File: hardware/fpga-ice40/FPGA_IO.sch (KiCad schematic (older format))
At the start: 1 part, among them U1 iCE40HX4K-TQ144

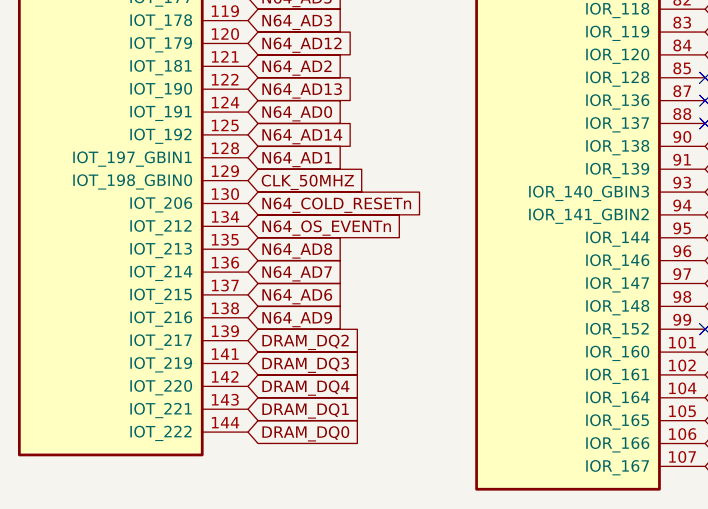
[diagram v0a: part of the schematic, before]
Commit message: Finish layout of power mux
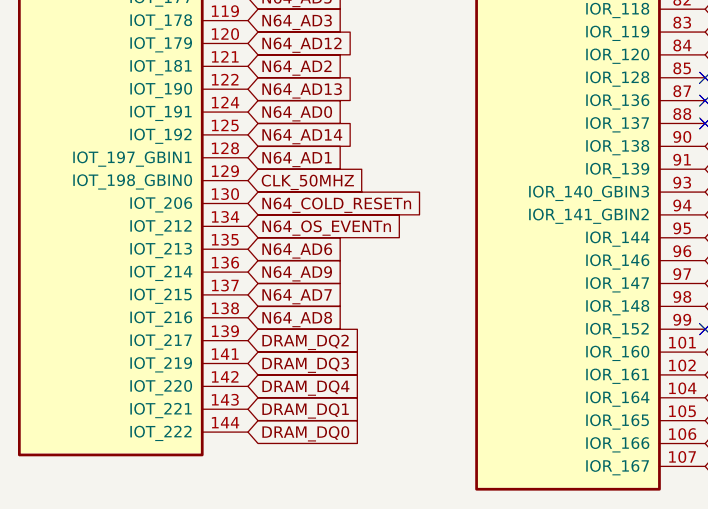
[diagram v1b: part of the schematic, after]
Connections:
- net N64_AD6: now also U1.135 (IOT_213); no longer U1.137 (IOT_215)
- net N64_AD7: now also U1.137 (IOT_215); no longer U1.136 (IOT_214)
- net N64_AD8: now also U1.138 (IOT_216); no longer U1.135 (IOT_213)
- net N64_AD9: now also U1.136 (IOT_214); no longer U1.138 (IOT_216)
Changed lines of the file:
@@
 Text GLabel 8850 3850 2    50   Input ~ 0
 DRAM_DQ8
-Text GLabel 2850 4750 2    50   Input ~ 0
+Text GLabel 2850 4850 2    50   Input ~ 0
 N64_AD7
-Text GLabel 2850 4850 2    50   Input ~ 0
+Text GLabel 2850 4650 2    50   Input ~ 0
 N64_AD6
 Text GLabel 2850 3550 2    50   Input ~ 0
@@
 Text GLabel 2850 4450 2    50   Input ~ 0
 N64_COLD_RESETn
-Text GLabel 2850 4650 2    50   Input ~ 0
+Text GLabel 2850 4950 2    50   Input ~ 0
 N64_AD8
-Text GLabel 2850 4950 2    50   Input ~ 0
+Text GLabel 2850 4750 2    50   Input ~ 0
 N64_AD9
 Text GLabel 2850 3450 2    50   Input ~ 0

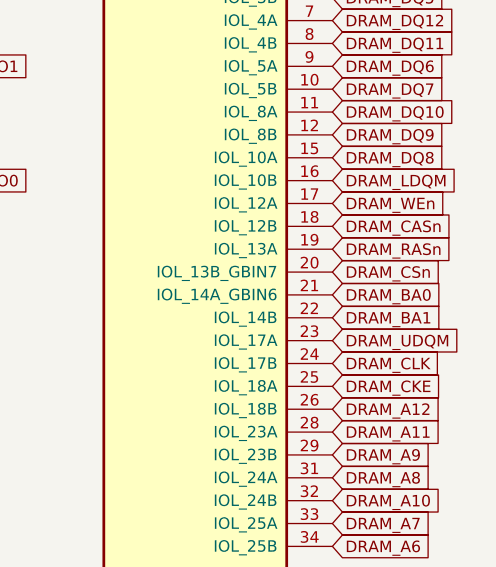
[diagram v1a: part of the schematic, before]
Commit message: Add series termination resistors to SDRAM bus
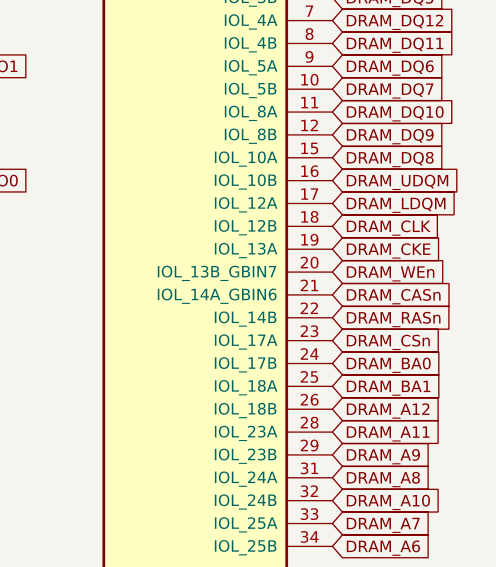
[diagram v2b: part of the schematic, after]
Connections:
- net DRAM_BA0: now also U1.24 (IOL_17B); no longer U1.21 (IOL_14A_GBIN6)
- net DRAM_BA1: now also U1.25 (IOL_18A); no longer U1.22 (IOL_14B)
- net DRAM_CASn: now also U1.21 (IOL_14A_GBIN6); no longer U1.18 (IOL_12B)
- net DRAM_CKE: now also U1.19 (IOL_13A); no longer U1.25 (IOL_18A)
- net DRAM_CLK: now also U1.18 (IOL_12B); no longer U1.24 (IOL_17B)
- net DRAM_CSn: now also U1.23 (IOL_17A); no longer U1.20 (IOL_13B_GBIN7)
- net DRAM_LDQM: now also U1.17 (IOL_12A); no longer U1.16 (IOL_10B)
- net DRAM_RASn: now also U1.22 (IOL_14B); no longer U1.19 (IOL_13A)
- net DRAM_UDQM: now also U1.16 (IOL_10B); no longer U1.23 (IOL_17A)
- net DRAM_WEn: now also U1.20 (IOL_13B_GBIN7); no longer U1.17 (IOL_12A)
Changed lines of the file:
@@
 Text GLabel 6850 2950 2    50   Input ~ 0
 DRAM_A5
+Text GLabel 8850 4850 2    50   Input ~ 0
+DRAM_BA1
+Text GLabel 8850 4750 2    50   Input ~ 0
+DRAM_BA0
+Text GLabel 8850 4650 2    50   Input ~ 0
+DRAM_CSn
 Text GLabel 8850 4550 2    50   Input ~ 0
-DRAM_BA1
+DRAM_RASn
 Text GLabel 8850 4450 2    50   Input ~ 0
-DRAM_BA0
+DRAM_CASn
 Text GLabel 8850 4350 2    50   Input ~ 0
-DRAM_CSn
-Text GLabel 8850 4250 2    50   Input ~ 0
-DRAM_RASn
-Text GLabel 8850 4150 2    50   Input ~ 0
-DRAM_CASn
+DRAM_WEn
 Text GLabel 8850 4050 2    50   Input ~ 0
-DRAM_WEn
-Text GLabel 8850 3950 2    50   Input ~ 0
 DRAM_LDQM
 Text GLabel 6850 3050 2    50   Input ~ 0
@@
 Text GLabel 6850 2850 2    50   Input ~ 0
 DRAM_A4
-Text GLabel 8850 4850 2    50   Input ~ 0
+Text GLabel 8850 4250 2    50   Input ~ 0
 DRAM_CKE
-Text GLabel 8850 4750 2    50   Input ~ 0
+Text GLabel 8850 4150 2    50   Input ~ 0
 DRAM_CLK
-Text GLabel 8850 4650 2    50   Input ~ 0
+Text GLabel 8850 3950 2    50   Input ~ 0
 DRAM_UDQM
 Text GLabel 8850 2850 2    50   Input ~ 0
